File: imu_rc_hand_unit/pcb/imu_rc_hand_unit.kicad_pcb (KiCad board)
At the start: 2 copper layers, 35 x 50 mm, 80 parts, among them J1 USB_C_Receptacle_USB2.0_16P, J2 JST SH1.0, Q1 IRLML6344TRPBF, Q2 IRLML6344TRPBF, Q3 DMP3160L-7, Q4 IRLML6344TRPBF, Q5 DMP3160L-7, Q6 BSS138, Q7 BC817-25, Q8 BC817-25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

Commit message: commit #27
revision for hand unit complete (board is ready)
board for proximity sensors in series
minor revision in encoder board
progressing work in car board
added essential libraries support for 3D components
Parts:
- J2: footprint Connector_JST:JST_SH_SM04B-SRSS-TB_1x04-1MP_P1.00mm_Horizontal -> IMURCLibrary:JST_SH_SM04B-SRSS-TB_1x04-1MP_P1.00mm_Horizontal
- moved R2 4.24 mm to (30.3, 58.9), turned to 0 degrees
- moved C1 3.59 mm to (27.0, 60.4), turned to 90 degrees
- moved C3 2.62 mm to (33.4, 57.3), turned to 90 degrees
- moved U6 2.55 mm to (37.6, 55.7)
- moved C2 1.82 mm to (32.7, 54.7)
- moved R1 1.42 mm to (41.9, 59.6), turned to 180 degrees
- moved R3 0.82 mm to (30.3, 56.7)
- moved D3 0.69 mm to (39.0, 59.9)
- moved D2 0.67 mm to (36.4, 59.9)
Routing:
- net VBUS: track 63.5 -> 69.0 mm
- net Net-(D3-A2): track 12.3 -> 9.15 mm
- net RTS: track 9.49 -> 12.5 mm
- net Net-(J1-CC1): track 4.72 -> 7.72 mm
- net Net-(U6-~{SUSPEND}): track 3.86 -> 6.39 mm
- net Net-(U6-~{RST}): track 3.91 -> 6.37 mm
- net U0RXD: track 9.45 -> 7.53 mm
- net DTR: track 13.3 -> 11.4 mm
- net Net-(D2-A2): track 12.1 -> 10.3 mm
- net U0TXD: track 10.6 -> 8.89 mm
- net Net-(U6-VBUS): track 12.4 -> 14.0 mm
- net Net-(D1-A2): track 12.9 -> 14.1 mm
- net GND: track 16.9 -> 17.6 mm, vias 166 -> 143
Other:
- board text removed: "{ "ViaStitching": "0.2", "stitch_zone_0": { "HSpacing": "1", "VSpacing": "1", "HOffset": "0", "VOffset": "0", "Clearance": "0.2", "Randomize": false } }"

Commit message: commit #28
added 3d file for esp32s3
progression with car pcb
minor changes prox sensors test board
final revision hand unit
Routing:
- net GND: vias 143 -> 208

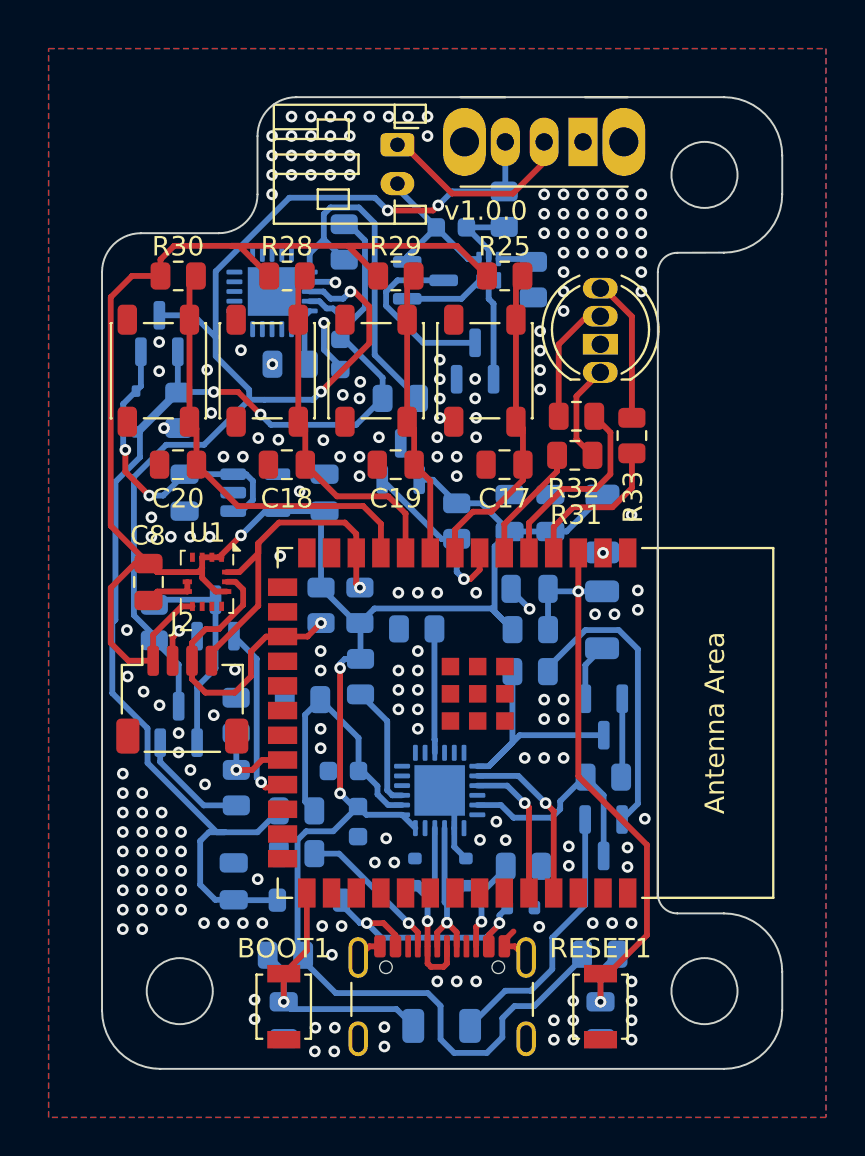
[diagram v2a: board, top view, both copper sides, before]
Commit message: commit #34
pcb hand unit v1.1.0:
chaged RGB led footprint to better fit
switch drain with source in Q5 MOSFET (battery reader)

pcb car v1.1.0:
removed power planes, added traces only
switch drain with source in Q1 MOSFET (battery reader)
changed LDO position

code:
changed esp32 devkit to esp32s3 devkit
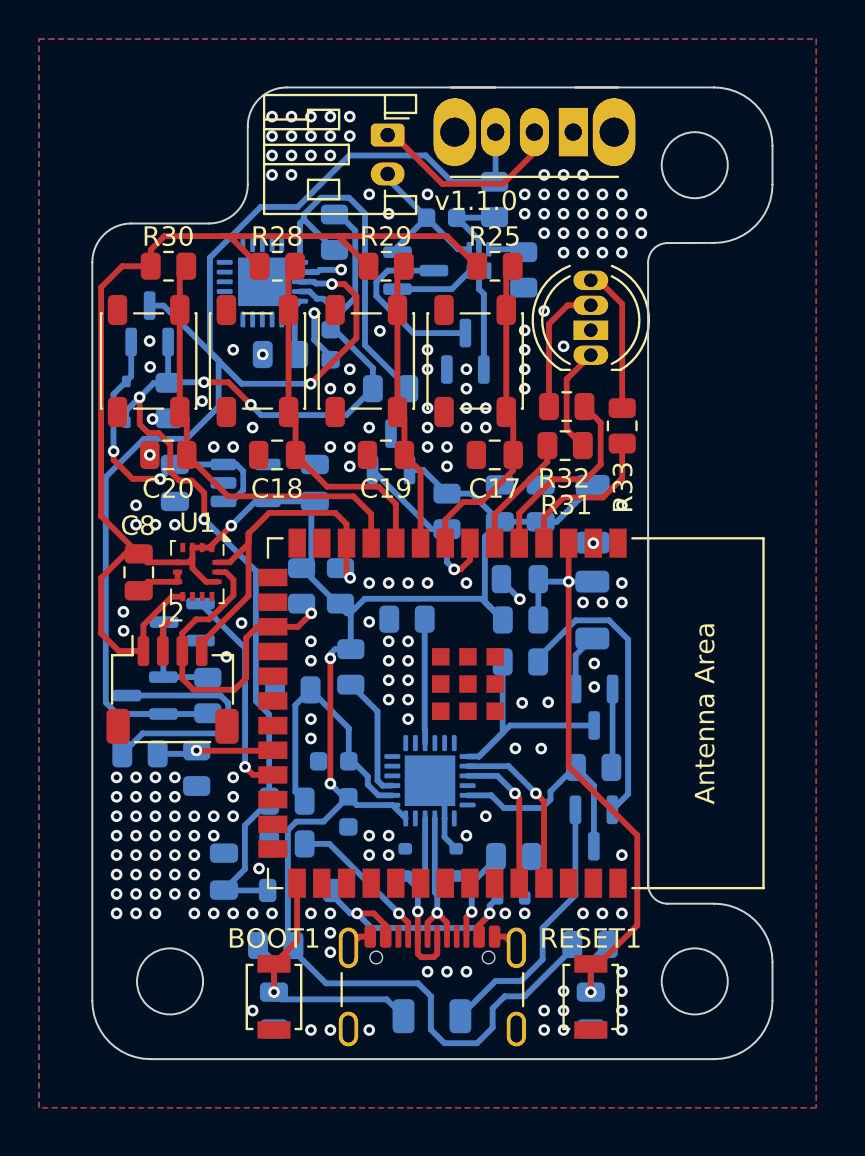
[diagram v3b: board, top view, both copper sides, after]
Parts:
- R1, R2: value 5k1 -> 5k1 (1%)
- R13: value 6k -> 3k (1%)
- R14: value 22k -> 11k (1%)
- R20, R21, R9: value 2k2 -> 2k2 (1%)
- moved R13 5.25 mm to (22.2, 53.8), turned to 0 degrees
- moved R12 4.65 mm to (25.7, 50.8)
- moved R14 3.39 mm to (25.1, 54.5), turned to -90 degrees
- moved Q5 2.28 mm to (22.5, 50.8), turned to 180 degrees
- moved Q4 1.72 mm to (24.4, 47.0), turned to 180 degrees
- moved R20 1.41 mm to (32.5, 45.1)
- moved R21 1.41 mm to (30.5, 45.1)
- moved R27 0.71 mm to (29.2, 63.6)
- moved BOOT1 0.71 mm to (29.1, 66.3)
- moved BT1 0.71 mm to (35.0, 21.9)
- moved C1 0.71 mm to (26.5, 59.9)
- moved C11 0.71 mm to (42.8, 40.9)
- moved C12 0.71 mm to (40.7, 40.9)
- moved C13 0.71 mm to (41.8, 44.8)
- moved C14 0.71 mm to (45.4, 67.0)
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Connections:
- Q5 pad 2: Net-(Q5-S) -> +BATT
- Q5 pad 3: +BATT -> Net-(Q5-D)
- R13 pad 1: Net-(Q5-S) -> Net-(Q5-D)
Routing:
- net Net-(Q5-D): track 0.00 -> 12.5 mm
- net +BATT: track 63.6 -> 70.9 mm, vias 4 -> 2
- net Net-(Q4-D): track 11.0 -> 5.14 mm
- net Net-(Q5-S): track 5.83 -> 0.00 mm
- net VBUS: track 69.0 -> 63.5 mm, vias 2 -> 4
- net BATT_READ_EN: track 9.40 -> 11.0 mm
- net BATT_READ: track 4.49 -> 6.01 mm
- net SCL: track 16.3 -> 17.3 mm
- net CHRG_5V: track 20.5 -> 21.3 mm
- net GND: track 17.6 -> 17.5 mm, vias 208 -> 202
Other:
- board text added: "v1.1.0"
- board text removed: "JLCJLCJLCJLC"
- board text removed: "v1.0.0"
